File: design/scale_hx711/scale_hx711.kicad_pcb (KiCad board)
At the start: 2 copper layers, 70 x 40 mm, 76 parts, among them J1 USB_B_Micro, J2 Conn_02x03_Odd_Even, J3 Load cell, Q1 IRLML6401, Q2 AO3400, Q3 BC857, SW1 SW_SPST, SW2 ON/OFF switch, U1 MDBT42Q, U2 BQ21040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

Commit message: PCB Files added, for scale_hx711
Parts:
- moved C29 55.5 mm to (51.8, 12.2), turned to 90 degrees
- moved R12 52.5 mm to (53.2, 25.8), turned to 180 degrees
- moved C32 51.5 mm to (49.7, 23.9), turned to 180 degrees
- moved L2 50.1 mm to (37.5, 35.5)
- moved L1 49.3 mm to (37.5, 37.2), turned to 180 degrees
- moved C30 48.1 mm to (49.7, 21.6), turned to 180 degrees
- moved Q3 47.5 mm to (73.5, 39.0)
- moved R13 46.5 mm to (53.2, 27.5), turned to 180 degrees
- moved R11 45.2 mm to (54.8, 12.2), turned to 90 degrees
- moved C1 41.2 mm to (37.5, 38.8)
- moved U5 41.2 mm to (58.3, 14.0)
- moved C31 41.1 mm to (55.7, 22.8), turned to 90 degrees
- moved C5 40.7 mm to (37.5, 32.4)
- moved C3 40.6 mm to (37.5, 33.8)
- moved C28 40.4 mm to (53.2, 12.2), turned to 90 degrees
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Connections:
- C8 pad 1: /nRF/VBAT -> /Sheet5E602498/VBAT
- EINK1 pad 10: (no net) -> /Sheet5E60241E/EINK_RST
- EINK1 pad 13: (no net) -> /Sheet5E60241E/EINK_SCLK
- EINK1 pad 14: (no net) -> /Sheet5E60241E/EINK_SDIO
- EINK1 pad 9: (no net) -> /Sheet5E60241E/EINK_BUSY
- J2 pad 2: /nRF/RX -> VDD
- J2 pad 4: VDD -> GND
- J2 pad 5: /nRF/TX -> /nRF/RX
- J2 pad 6: GND -> /nRF/TX
- Q1 pad 2: /nRF/VBAT -> /Sheet5E602498/VBAT
- U1 pad 18: (no net) -> /Sheet5E602498/Vlc
- U1 pad 2: (no net) -> /Sheet5E60241E/EINK_BUSY
- U1 pad 20: (no net) -> /Sheet5E602498/10V_LDO_EN
- U1 pad 21: (no net) -> /Sheet5E602498/BOOST_EN
- U1 pad 25: (no net) -> /Sheet5E602498/HX711_RATE
- U1 pad 26: (no net) -> /Sheet5E602498/HX711_DATA
- U1 pad 27: (no net) -> /Sheet5E602498/HX711_CLK
- U1 pad 3: (no net) -> /Sheet5E60241E/EINK_RST
- U1 pad 4: (no net) -> /Sheet5E60241E/EINK_CS
- U1 pad 5: (no net) -> /Sheet5E60241E/EINK_SCLK
- U1 pad 6: (no net) -> /Sheet5E60241E/EINK_SDIO
- U3 pad 1: /nRF/VBAT -> /Sheet5E602498/VBAT
- U3 pad 3: /nRF/VBAT -> /Sheet5E602498/VBAT
- U4 pad 11: (no net) -> /Sheet5E602498/HX711_CLK
- U4 pad 12: (no net) -> /Sheet5E602498/HX711_DATA
- U4 pad 15: (no net) -> /Sheet5E602498/HX711_RATE
- U5 pad 4: (no net) -> /Sheet5E602498/BOOST_EN
- U6 pad 3: (no net) -> /Sheet5E602498/10V_LDO_EN
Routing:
- net VDD: track 0.00 -> 128.6 mm, vias 0 -> 4
- net GND: track 0.00 -> 107.3 mm, vias 0 -> 33
- net /Sheet5E602498/VSUP: track 0.00 -> 52.1 mm, vias 0 -> 2
- net Net-(BT1-Pad1): track 0.00 -> 47.9 mm, vias 0 -> 1
- net Net-(Q1-Pad3): track 0.00 -> 31.3 mm, vias 0 -> 1
- net /Sheet5E60241E/EINK_BUSY: track 0.00 -> 30.7 mm
- net /Sheet5E60241E/EINK_RST: track 0.00 -> 29.8 mm
- net /Sheet5E60241E/EINK_CS: track 0.00 -> 28.9 mm
- net /Sheet5E60241E/RESE: track 0.00 -> 28.8 mm, vias 0 -> 2
- net /Sheet5E602498/BOOST_EN: track 0.00 -> 28.1 mm, vias 0 -> 2
- net /Sheet5E602498/HX711_RATE: track 0.00 -> 27.7 mm
- net /Sheet5E60241E/EINK_SCLK: track 0.00 -> 27.4 mm
- net /nRF/BUTTON: track 0.00 -> 27.1 mm, vias 0 -> 1
- net /Sheet5E60241E/GDR: track 0.00 -> 26.8 mm
- net /Sheet5E60241E/EINK_SDIO: track 0.00 -> 26.0 mm
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- added copper zone on B.Cu, net GND
- added copper zone on F.Cu, net GND
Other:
- outline, holes or cut-outs redrawn

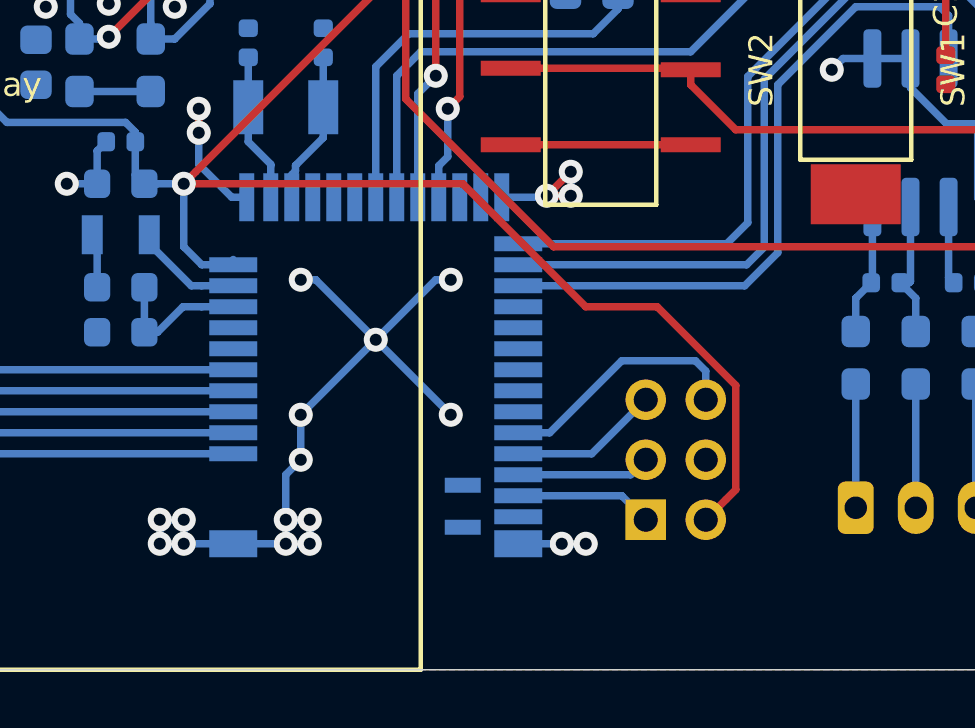
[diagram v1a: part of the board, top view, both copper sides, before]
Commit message: Adds extra GPIO pins for nrf in scale_hx711
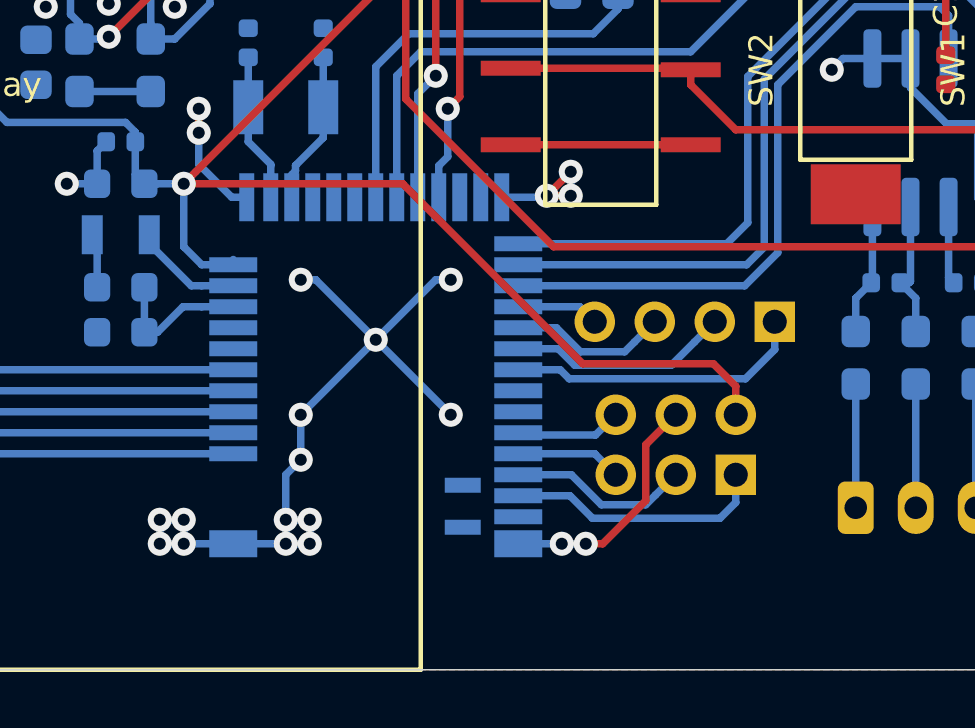
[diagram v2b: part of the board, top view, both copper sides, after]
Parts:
- added J4: Conn_01x04, Connector_PinHeader_2.00mm:PinHeader_1x04_P2.00mm_Vertical, B.Cu at (59.3, 38.4)
- moved J2 3.35 mm to (58.0, 43.5), turned to 90 degrees
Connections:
- U1 pad 28: (no net) -> /nRF/GPIO3
- U1 pad 29: (no net) -> /nRF/GPIO2
- U1 pad 30: (no net) -> /nRF/GPIO1
- U1 pad 31: (no net) -> /nRF/GPIO0
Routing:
- net /nRF/GPIO0: track 0.00 -> 10.0 mm
- net /nRF/GPIO1: track 0.00 -> 7.38 mm
- net GND: track 107.3 -> 113.2 mm
- net /nRF/GPIO2: track 0.00 -> 5.30 mm
- net /nRF/TX: track 8.34 -> 3.56 mm
- net /nRF/SWDIO: track 4.58 -> 8.70 mm
- net VDD: track 128.6 -> 124.7 mm
- net /nRF/GPIO3: track 0.00 -> 2.76 mm
- net /nRF/SWDCLK: track 4.46 -> 6.08 mm
- net /nRF/RX: track 5.00 -> 3.54 mm

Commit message: BOMs, schematics updated, scale_ltc6915 PCB Design complete.
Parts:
- added Q4: AO3400, Package_TO_SOT_SMD:SOT-23, B.Cu at (56.4, 30.5)
- added R14: 10k, Resistor_SMD:R_0603_1608Metric_Pad1.05x0.95mm_HandSolder, B.Cu at (49.8, 29.8)
- added R15: 10k, Resistor_SMD:R_0603_1608Metric_Pad1.05x0.95mm_HandSolder, B.Cu at (53.1, 29.8)
- R5: footprint Resistor_SMD:R_0603_1608Metric_Pad1.05x0.95mm_HandSolder -> Resistor_SMD:R_1206_3216Metric
- R6: value 100 -> 4.7k
- R7: value 100 -> 24k
- moved R4 1.60 mm to (41.0, 13.5)
- moved R5 0.32 mm to (44.5, 12.5), turned to 180 degrees
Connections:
- U1 pad 17: (no net) -> /Sheet5E602498/Vlc
- U1 pad 18: /Sheet5E602498/Vlc -> /nRF/BT_LV
- U1 pad 19: /nRF/BUTTON -> (no net)
- U1 pad 20: /Sheet5E602498/10V_LDO_EN -> /nRF/BUTTON
- U1 pad 21: /Sheet5E602498/BOOST_EN -> /Sheet5E602498/10V_LDO_EN
- U1 pad 22: (no net) -> /Sheet5E602498/BOOST_EN
- U1 pad 23: (no net) -> /nRF/BT_LV_EN
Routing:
- net GND: track 113.2 -> 141.8 mm, vias 33 -> 36
- net /Sheet5E602498/VBAT: track 21.9 -> 42.6 mm, vias 0 -> 2
- net /nRF/BT_LV: track 0.00 -> 12.0 mm
- net /nRF/BT_LV_EN: track 0.00 -> 10.7 mm
- net /nRF/BUTTON: track 27.1 -> 34.3 mm, vias 1 -> 3
- net /Sheet5E602498/10V_LDO_EN: track 18.5 -> 23.0 mm
- net /Sheet5E60241E/RESE: track 28.8 -> 31.9 mm, vias 2 -> 0
- net Net-(Q4-Pad3): track 0.00 -> 1.71 mm
- net /Sheet5E602498/Vlc: track 15.4 -> 16.6 mm
- net VDD: track 124.7 -> 124.0 mm
- net /Sheet5E60241E/GDR: track 26.8 -> 26.4 mm, vias 0 -> 2
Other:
- board text added: "scale_hx711 PCB rev1"

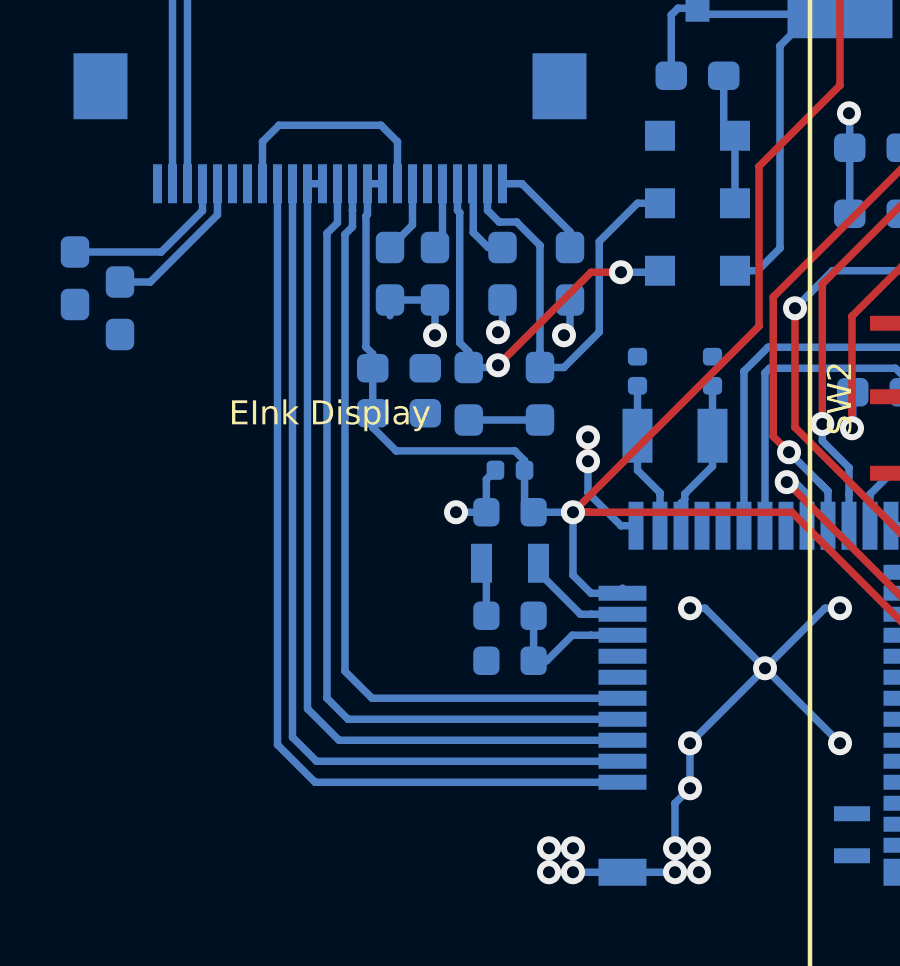
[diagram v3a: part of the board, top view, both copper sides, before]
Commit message: DC, CS pins separated, issue fixed. In both scale_hx711 and scale_ltc6915.
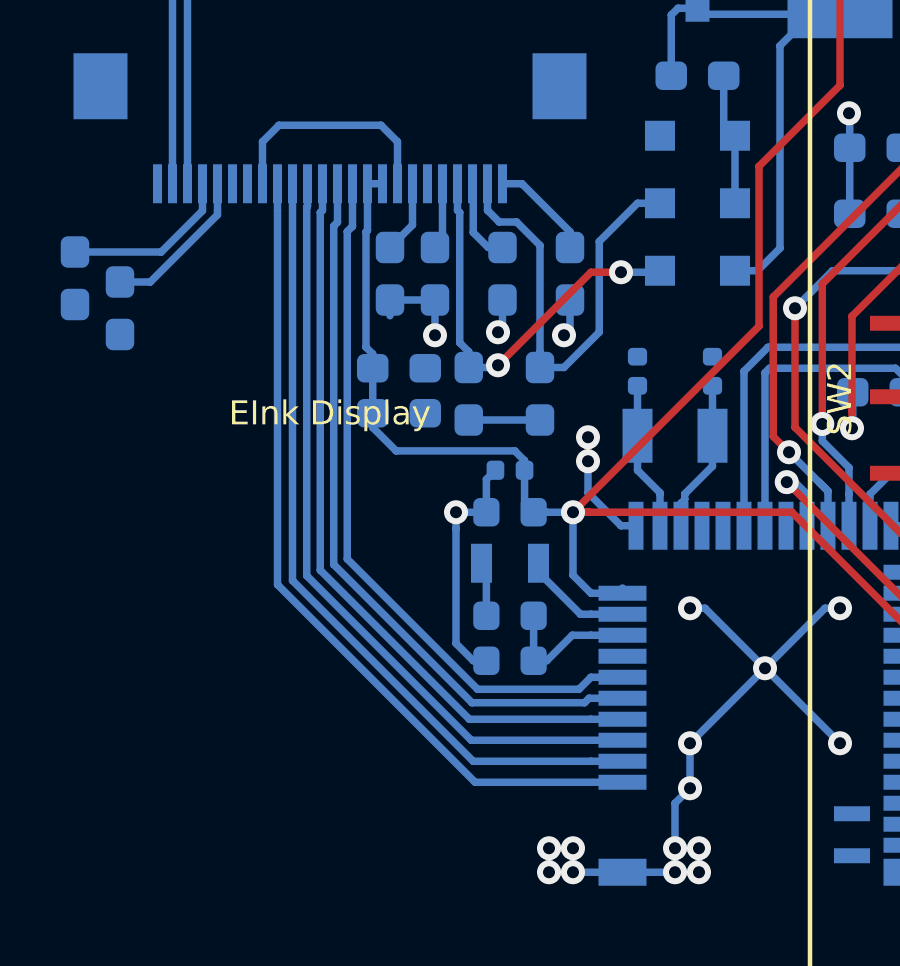
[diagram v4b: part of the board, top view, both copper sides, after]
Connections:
- EINK1 pad 11: /Sheet5E60241E/EINK_CS -> /Sheet5E60241E/EINK_DC
- U1 pad 4: /Sheet5E60241E/EINK_CS -> /Sheet5E60241E/EINK_DC
- U1 pad 5: /Sheet5E60241E/EINK_SCLK -> /Sheet5E60241E/EINK_CS
- U1 pad 6: /Sheet5E60241E/EINK_SDIO -> /Sheet5E60241E/EINK_SCLK
- U1 pad 7: (no net) -> /Sheet5E60241E/EINK_SDIO
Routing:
- net /Sheet5E60241E/EINK_DC: track 0.00 -> 25.9 mm
- net GND: track 141.8 -> 147.4 mm
- net /Sheet5E60241E/EINK_CS: track 28.9 -> 25.0 mm
- net /Sheet5E60241E/EINK_BUSY: track 30.7 -> 27.6 mm
- net /Sheet5E60241E/EINK_SCLK: track 27.4 -> 24.3 mm
- net /Sheet5E60241E/EINK_RST: track 29.8 -> 26.7 mm
- net /Sheet5E60241E/EINK_SDIO: track 26.0 -> 23.7 mm
